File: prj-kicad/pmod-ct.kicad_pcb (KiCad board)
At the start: 2 copper layers, 38.1 x 20.3 mm, 22 parts, among them P1 PMOD, P2 CONN_2, U1 MCP3201, U2 MCP6001

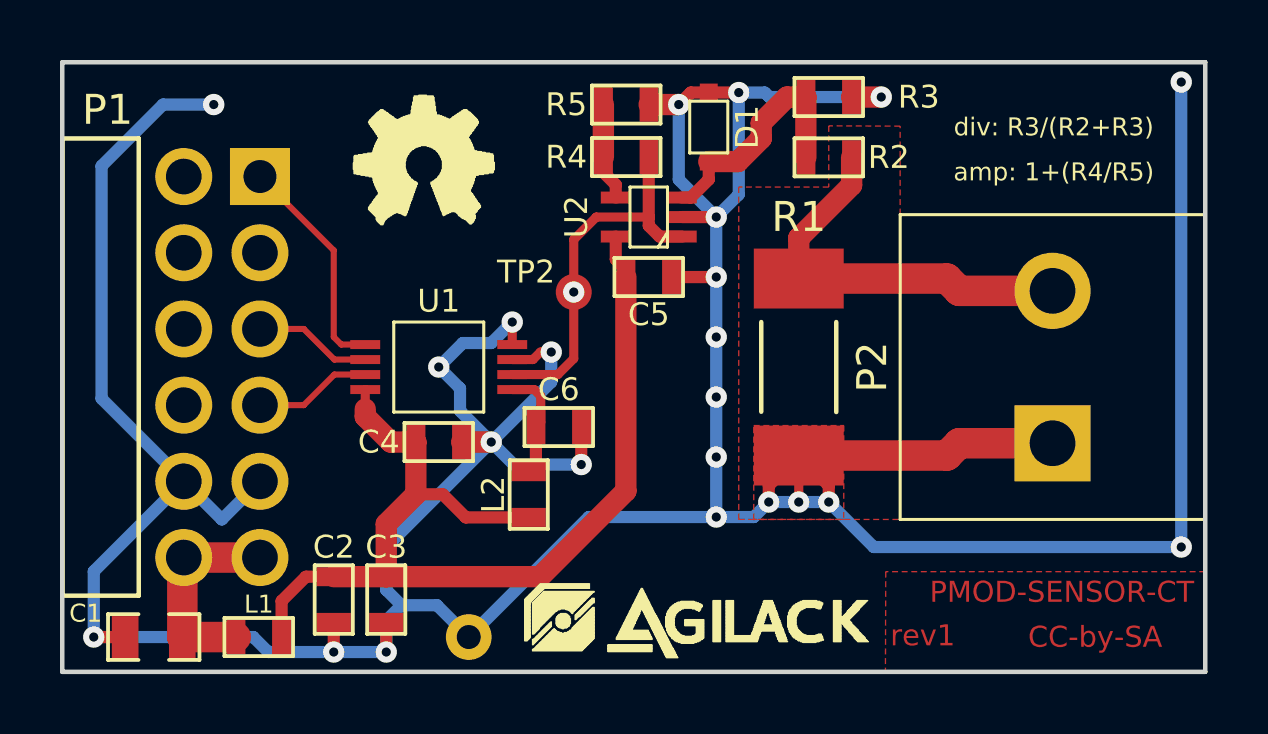
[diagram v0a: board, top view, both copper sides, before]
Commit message: Start rev2 design - Add voltage offset (VREF/2) for the burden resistor
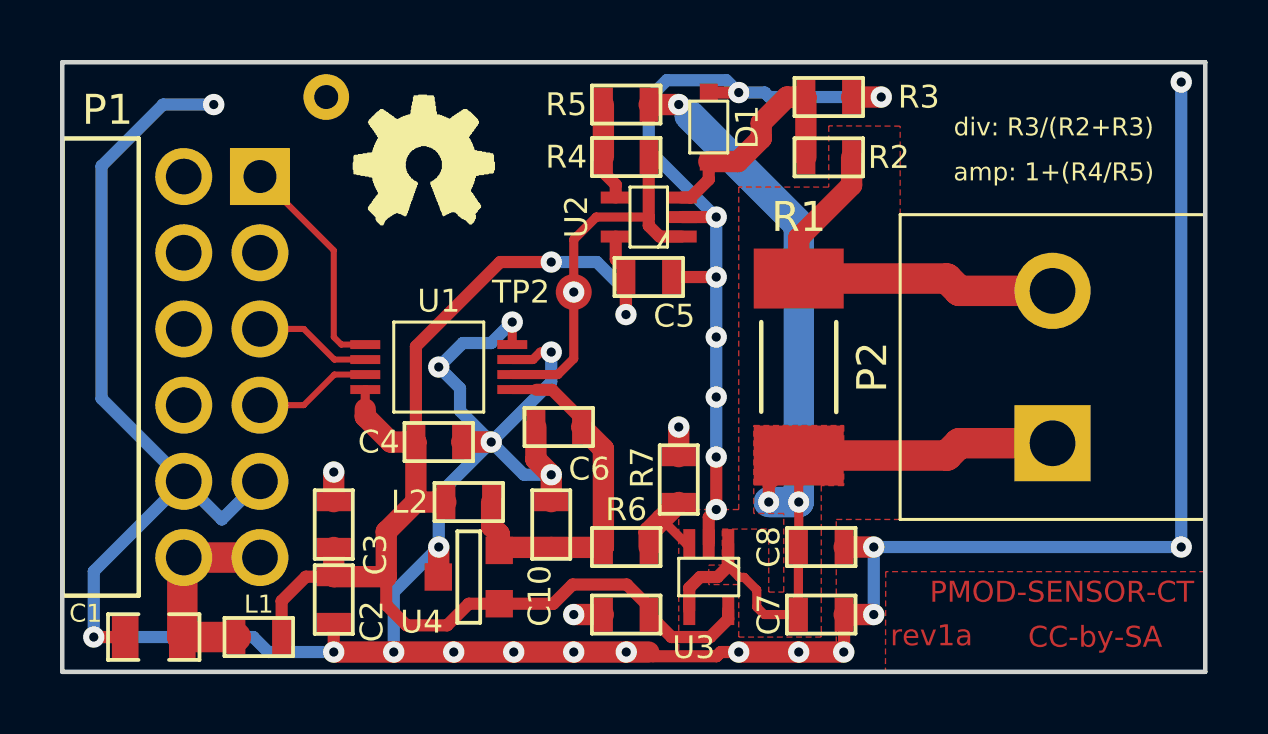
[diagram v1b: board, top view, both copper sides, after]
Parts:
- removed agilack-11.5: 450px, pmod-ct:logo-agilack-11.5
- added C10: 100nF, pmod-ct:SMD0603, F.Cu at (145.8, 110.2)
- added C7: 4,7uF, pmod-ct:SMD0603, F.Cu at (154.8, 113.2)
- added C8: 470pF, pmod-ct:SMD0603, F.Cu at (154.8, 111.0)
- added C9: 100nF, pmod-ct:SMD0603, F.Cu at (148.2, 113.2)
- added R6: 10k, pmod-ct:SMD0603, F.Cu at (148.2, 111.0)
- added R7: 10k, pmod-ct:SMD0603, F.Cu at (150.0, 108.8)
- added U3: MCP6001, pmod-ct:SC70-5, F.Cu at (151.0, 112.0)
- added U4: REF30xx, pmod-ct:SOT23-3, F.Cu at (143.0, 112.0)
- moved TP1 18.6 mm to (138.2, 96.0)
- moved C3 3.05 mm to (138.5, 110.2), turned to 90 degrees
- moved L2 2.02 mm to (143.0, 109.5), turned to 0 degrees
- turned C6 to 180 degrees
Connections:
- P2 pad 1: GND -> /VREF\2
- R1 pad 2: GND -> /VREF\2
- R5 pad 2: GND -> /VREF\2
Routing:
- net /VREF\2: track 0.00 -> 39.2 mm, vias 0 -> 3
- net +3.3V: track 35.1 -> 45.1 mm, vias 0 -> 2
- net GND: track 154.8 -> 145.8 mm, vias 23 -> 32
- net +VRef: track 3.72 -> 12.5 mm
- net Net-(R6-Pad1): track 0.00 -> 3.15 mm
- added copper zone on F.Cu, net /VREF\2
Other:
- board text added: "rev1a"
- board text removed: "rev1"

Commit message: Rev2: PCB is now 4 layers ; add a switch to control input divider
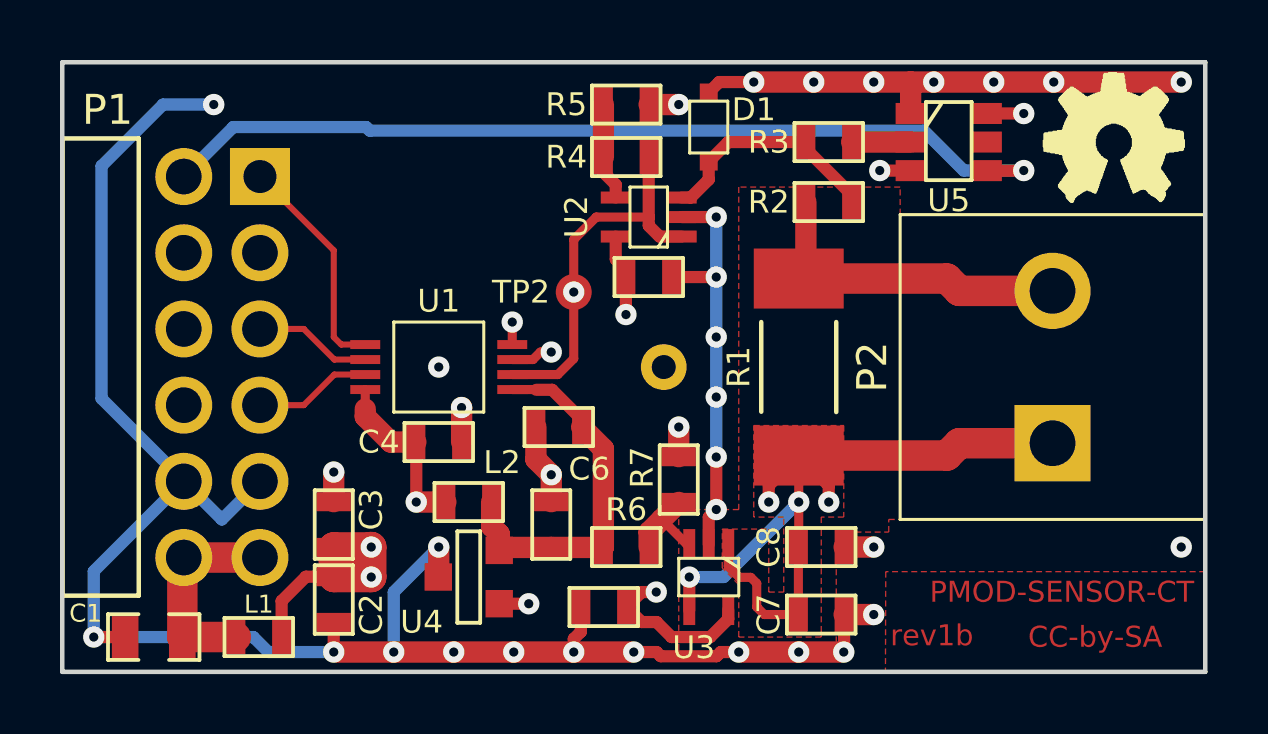
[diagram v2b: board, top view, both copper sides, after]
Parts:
- added U5: ADG802, pmod-ct:SOT23-6, F.Cu at (159.0, 97.5)
- moved ohw_logo 23.0 mm to (164.5, 97.5)
- moved TP1 14.4 mm to (149.5, 105.0)
- moved R3 1.50 mm to (155.0, 97.5)
- moved R2 1.49 mm to (155.0, 99.5)
- moved C9 0.79 mm to (147.5, 113.0)
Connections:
- P1 pad 7: Net-(P1-Pad7) -> DIV
- R2 pad 1: Net-(P2-Pad2) -> Net-(D1-Pad2)
- R2 pad 2: Net-(D1-Pad2) -> Net-(P2-Pad2)
- R3 pad 2: GND -> Net-(R3-Pad2)
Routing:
- net DIV: track 0.00 -> 30.5 mm, vias 0 -> 1
- net +3.3V: track 45.1 -> 73.1 mm, vias 2 -> 7
- net GND: track 145.8 -> 156.6 mm, vias 32 -> 36
- net /VREF\2: track 39.2 -> 43.8 mm, vias 3 -> 5
- net Net-(P2-Pad2): track 13.4 -> 11.3 mm
- net Net-(R3-Pad2): track 0.00 -> 1.97 mm
- added copper zone on In2.Cu, net +3.3V
- added copper zone on In2.Cu, net /VREF\2
- added copper zone on In1.Cu, net GND
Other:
- copper layers 2 -> 4
- board text added: "rev1b"
- board text removed: "rev1a"

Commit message: Rev2: Add a switch to control amplifier gain (G=1 or G=~10)
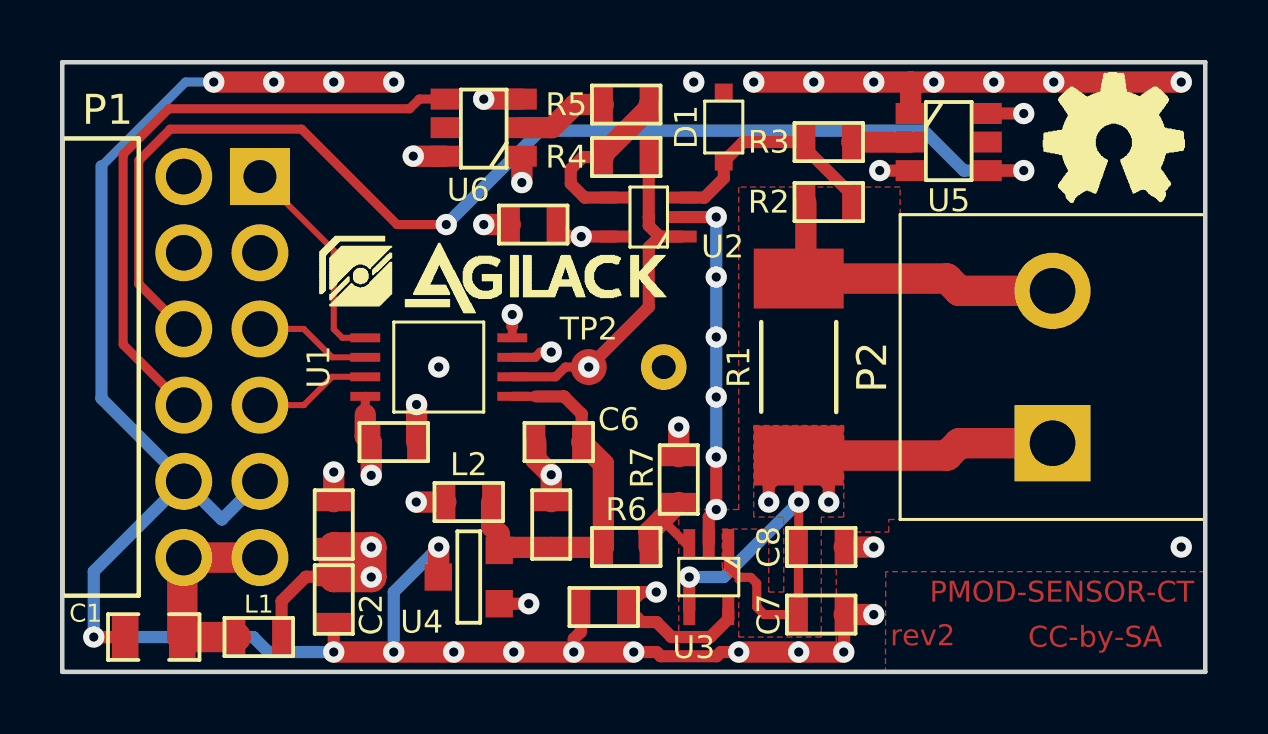
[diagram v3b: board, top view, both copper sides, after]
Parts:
- added U6: ADG802, pmod-ct:SOT23-6, F.Cu at (143.5, 97.0)
- added agilack-11.5: 450px, pmod-ct:logo-agilack-11.5, F.Cu at (144.2, 102.0)
- moved C5 4.23 mm to (145.2, 100.2), turned to 180 degrees
- moved TP2 2.55 mm to (147.0, 105.0)
- moved C4 1.50 mm to (140.5, 107.5)
- moved C6 0.50 mm to (146.0, 107.5)
- moved D1 0.50 mm to (151.5, 97.0)
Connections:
- P1 pad 10: Net-(P1-Pad10) -> AMP
- P1 pad 7: DIV -> Net-(P1-Pad7)
- P1 pad 9: Net-(P1-Pad9) -> DIV
- R5 pad 1: Net-(R4-Pad1) -> Net-(R5-Pad1)
- R5 pad 2: /VREF\2 -> Net-(R4-Pad1)
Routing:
- net AMP: track 0.00 -> 20.7 mm
- net +3.3V: track 73.1 -> 85.7 mm, vias 7 -> 9
- net DIV: track 30.5 -> 40.6 mm, vias 1 -> 2
- net GND: track 156.6 -> 162.4 mm, vias 36 -> 42
- net /VREF\2: track 43.8 -> 47.8 mm
- net Net-(R5-Pad1): track 0.00 -> 3.04 mm
- net Net-(R4-Pad1): track 3.27 -> 5.82 mm
- net Net-(R4-Pad2): track 12.6 -> 11.6 mm
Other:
- board text added: "rev2"
- board text removed: "rev1b"
